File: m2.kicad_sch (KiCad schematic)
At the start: 16 parts, among them M2 M2_2280, U15 MDT580M01001

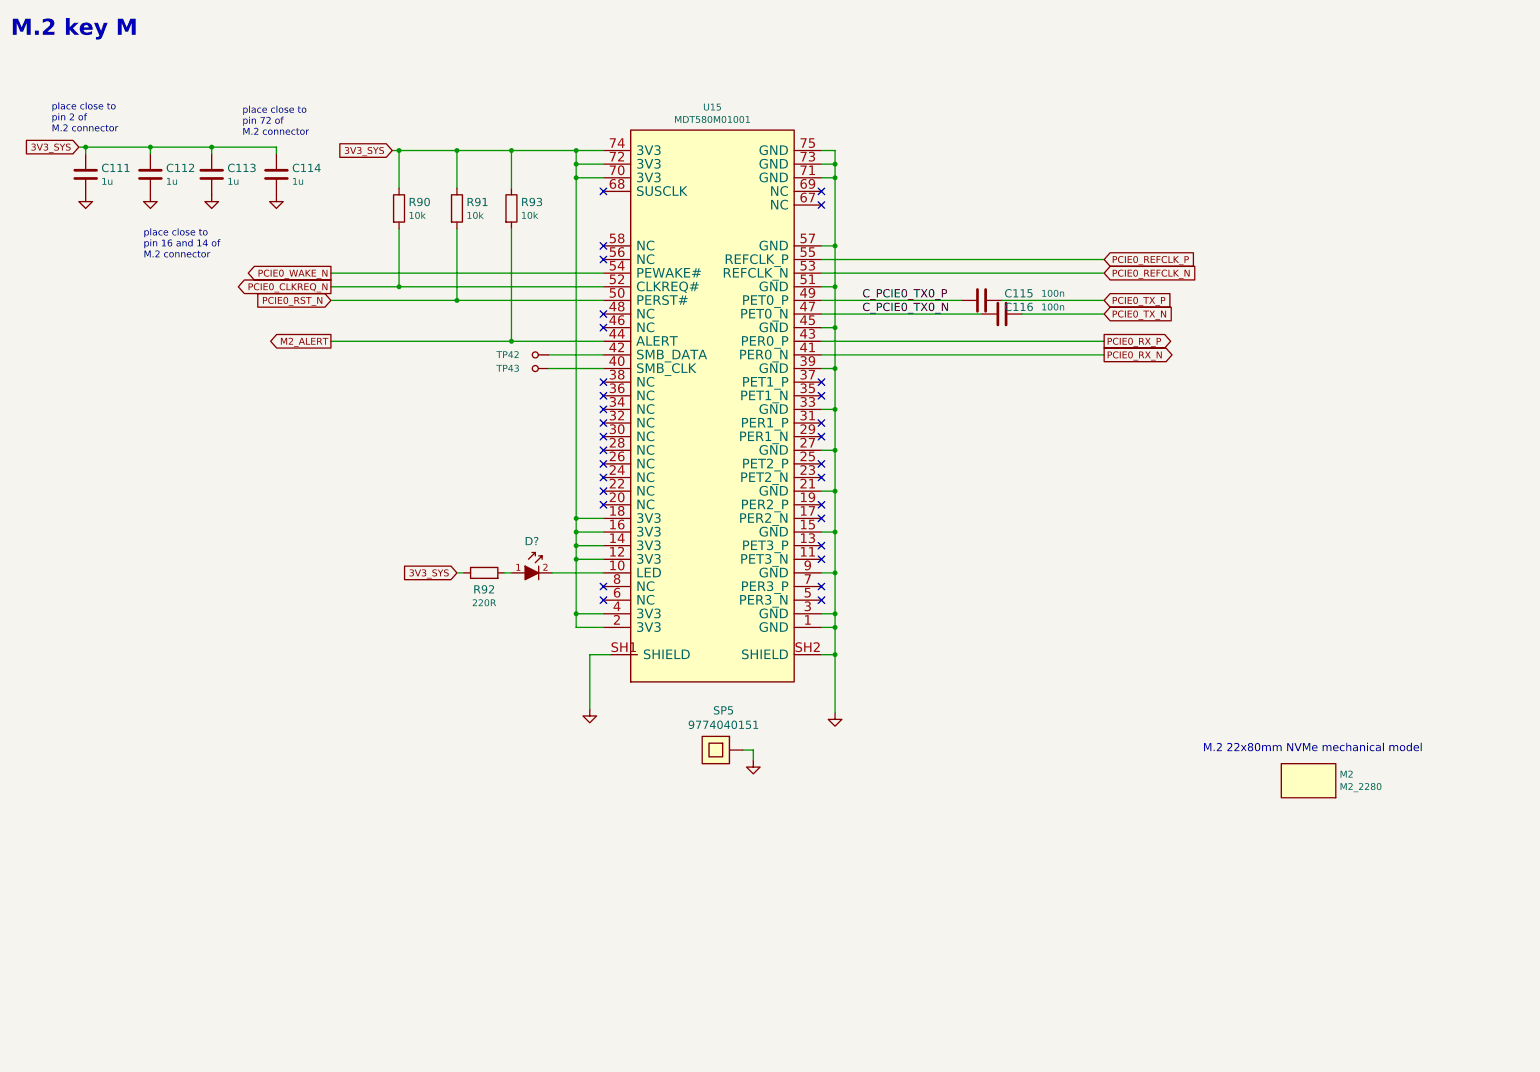
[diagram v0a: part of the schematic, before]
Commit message: Introduce component standardization
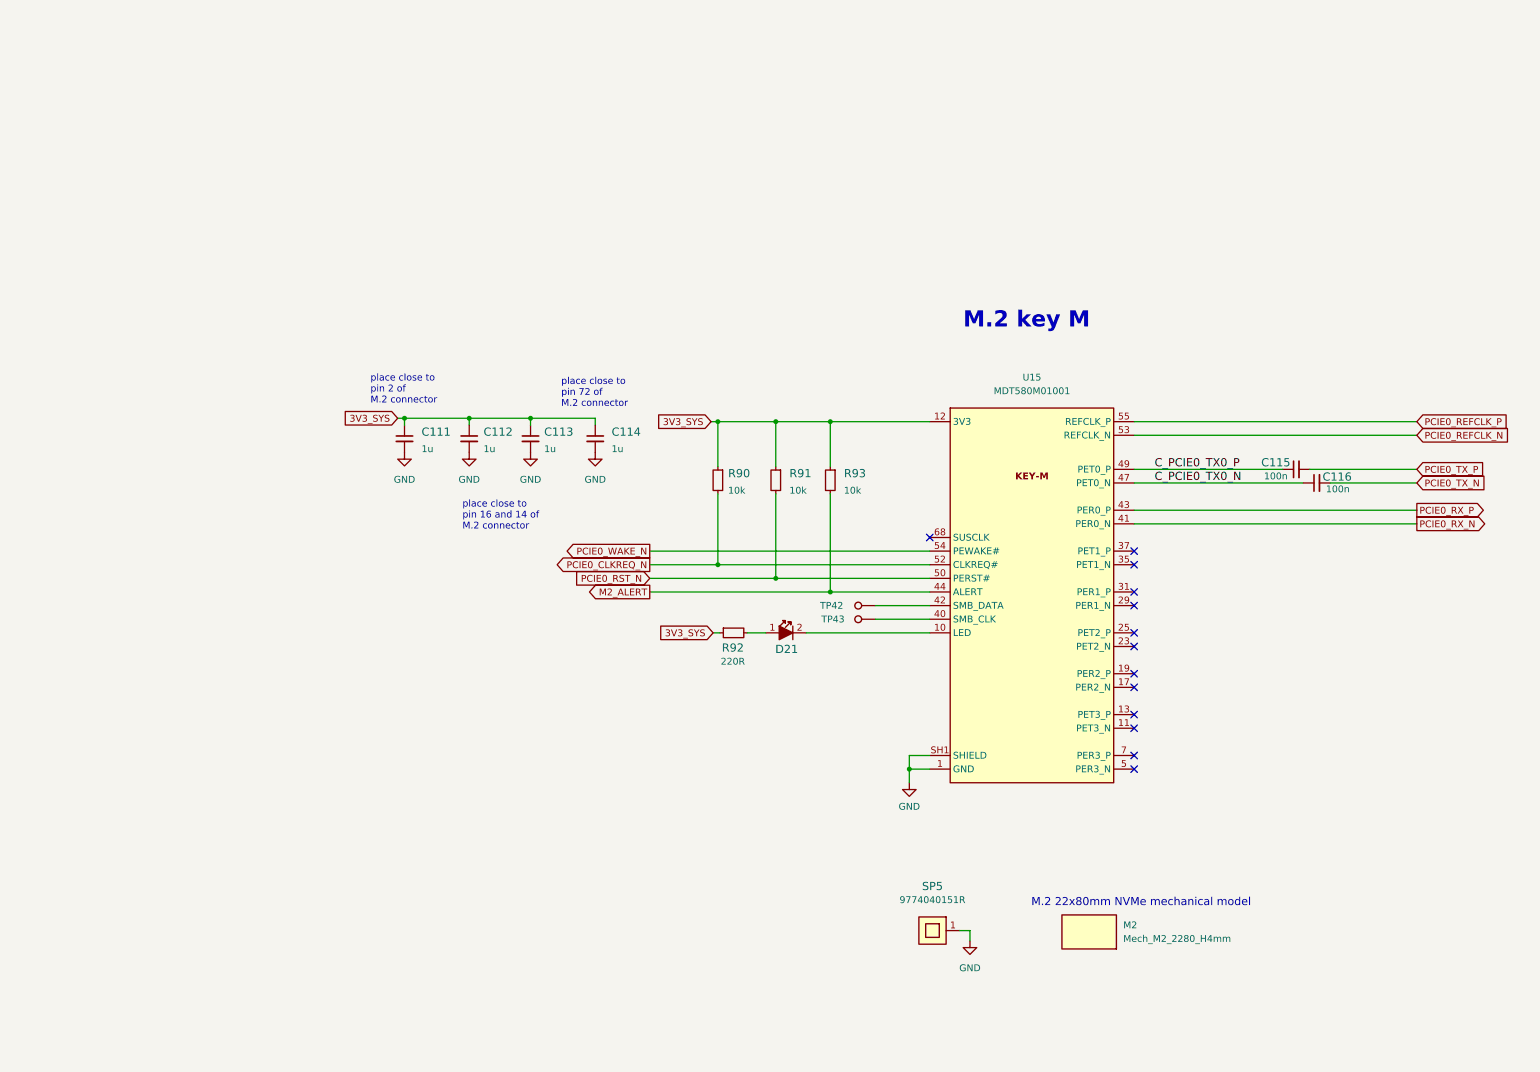
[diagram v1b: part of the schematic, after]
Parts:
- C111, C112, C113, C114: footprint sa800u-baseboard-hw-footprints:0402-cap -> sa800u-baseboard-hw-footprints:C_0402_1005Metric; Author (none) -> Antmicro; License (none) -> Apache-2.0
- C115, C116: footprint sa800u-baseboard-hw-footprints:0402-cap -> sa800u-baseboard-hw-footprints:C_0402_1005Metric; Author (none) -> Antmicro; Dielectric (none) -> X5R; License (none) -> Apache-2.0; MPN 0402X104K6R3CT -> GRM155R61H104KE14D; Manufacturer Walsin -> Murata; Voltage (none) -> 50V
- D21: renamed from D?; value (none) -> KP-1608EC; footprint (none) -> sa800u-baseboard-hw-footprints:LED_0603_1608Metric_G; symbol sa800u-baseboard-hw:KP-1608EC -> sa800u-baseboard-hw:LED_G_0603_KP-1608ZGC; Author (none) -> Antmicro; License (none) -> Apache-2.0; MPN KP-1608EC -> KP-1608ZGC; Manufacturer KINGBRIGHT -> Kingbright
- M2: value M2_2280 -> Mech_M2_2280_H4mm; footprint sa800u-baseboard-hw-footprints:m2_2280 -> sa800u-baseboard-hw-footprints:Mech_M2_2280_H4mm; symbol sa800u-baseboard-hw:M2_2280 -> sa800u-baseboard-hw:Mech_M2_2280_H4mm; Author (none) -> Antmicro; DNP (none) -> DNP; License (none) -> Apache-2.0
- R90, R91, R93: footprint sa800u-baseboard-hw-footprints:0402-res -> sa800u-baseboard-hw-footprints:R_0402_1005Metric; Author (none) -> Antmicro; License (none) -> Apache-2.0; MPN CRCW040210K0FKEDHP -> CR0402-FX-1002GLF; Manufacturer VISHAY -> Bourns; Tolerance (none) -> 1%
- R92: footprint sa800u-baseboard-hw-footprints:0402-res -> sa800u-baseboard-hw-footprints:R_0402_1005Metric; Author (none) -> Antmicro; License (none) -> Apache-2.0; MPN ERJ2GEJ221X -> CR0402-FX-2200GLF; Manufacturer Panasonic -> Bourns; Tolerance (none) -> 1%
- SP5: value 9774040151 -> Spacer_H4.0mm_9774040151; footprint sa800u-baseboard-hw-footprints:9774040151 -> sa800u-baseboard-hw-footprints:Spacer_SMD_M2.5_H4mm_Wurth_9774040151; symbol sa800u-baseboard-hw:9774040151 -> sa800u-baseboard-hw:Spacer_H4.0mm_9774040151; Author (none) -> Antmicro; License (none) -> Apache-2.0; MPN 9774030151 -> 9774040151R; Manufacturer Wurth Elektronik -> Würth Elektronik
- TP42, TP43: value TP_SMD_0_75MM -> TP_0.75mm_SMD; footprint sa800u-baseboard-hw-footprints:Testpoint_smd_0_75mm -> sa800u-baseboard-hw-footprints:TP_SMD_0.75mm; symbol sa800u-baseboard-hw:TP_SMD_0_75MM -> sa800u-baseboard-hw:TP_0.75mm_SMD; Author (none) -> Antmicro; License (none) -> Apache-2.0
- U15: value MDT580M01001 -> Bus_M.2_MDT580M01001; footprint sa800u-baseboard-hw-footprints:MDT580M01001 -> sa800u-baseboard-hw-footprints:Bus_M.2_Socket_Key_M_Amphenol_MDT580M01001; symbol sa800u-baseboard-hw:MDT580M01001 -> sa800u-baseboard-hw:Bus_M.2_MDT580M01001; Author (none) -> Antmicro; License (none) -> Apache-2.0; Manufacturer Amphenol FCI -> Amphenol
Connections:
- net at U15.20 (NC): now also U15.22 (NC), U15.24 (NC), U15.26 (NC), U15.28 (NC), U15.30 (NC), U15.32 (NC), U15.34 (NC), U15.36 (NC), U15.38 (NC), U15.46 (NC), U15.48 (NC), U15.56 (NC), U15.58 (NC), U15.6 (NC), U15.67 (NC), U15.69 (NC), U15.8 (NC)
- no-connect marks 31 -> 13
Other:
- moved on the sheet: C111, C112, C113, C114, C115, C116, M2, R90, R91, R92, R93, TP42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

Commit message: Add OHP assets
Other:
- company: (none) -> Antmicro Ltd.
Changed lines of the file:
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@@
   (title_block
     (title "SA800U (Snapdragon 845) Baseboard")
-    (date "2023-07-27")
-    (rev "1.0.2")
+    (date "2023-10-19")
+    (rev "1.0.3")
+    (company "Antmicro Ltd.")
     (comment 1 "www.antmicro.com")
-    (comment 2 "Antmicro Ltd.")
   )
   (junction (at 148.971 121.031) (diameter 0) (color 0 0 0 0)
